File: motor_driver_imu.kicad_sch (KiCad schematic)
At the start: 27 parts, among them M1 Motor_DC, M2 Motor_DC, M3 Motor_DC, M4 Motor_DC, Q1 AO3400A, Q2 AO3400A, Q3 AO3400A, Q4 AO3400A, U5 ICM-45605

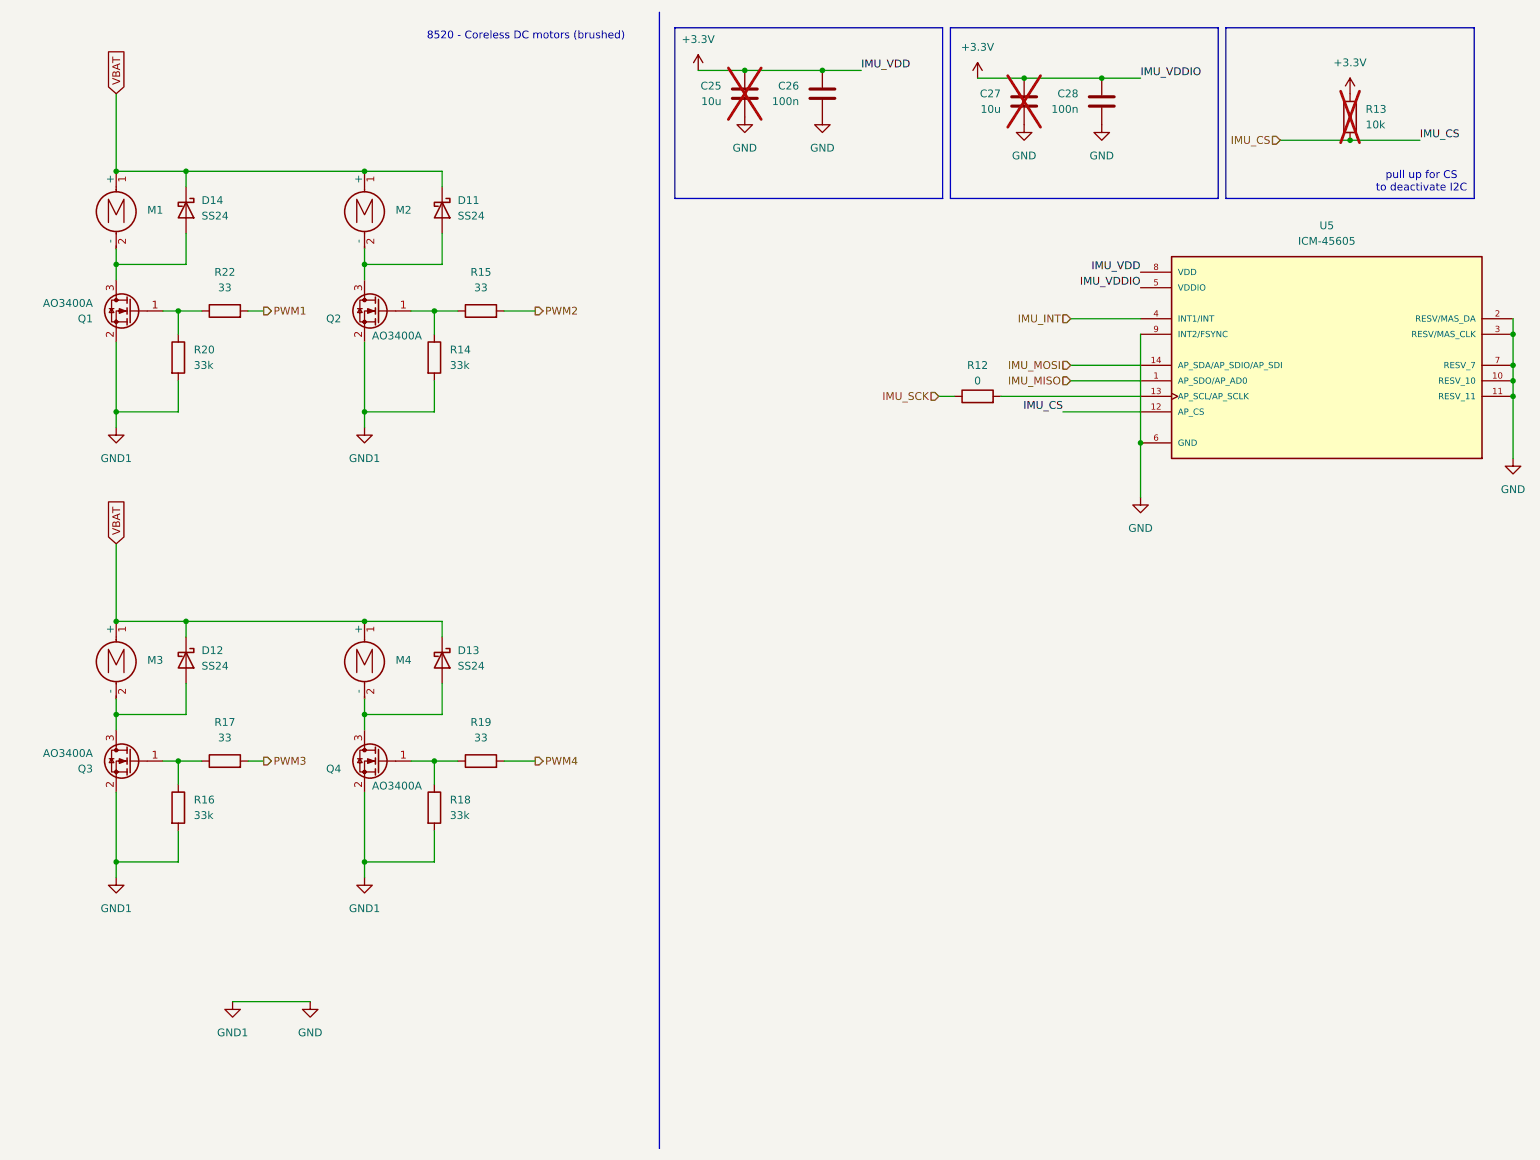
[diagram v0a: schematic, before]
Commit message: added 3.3 header for rx and changed flywheel diodes
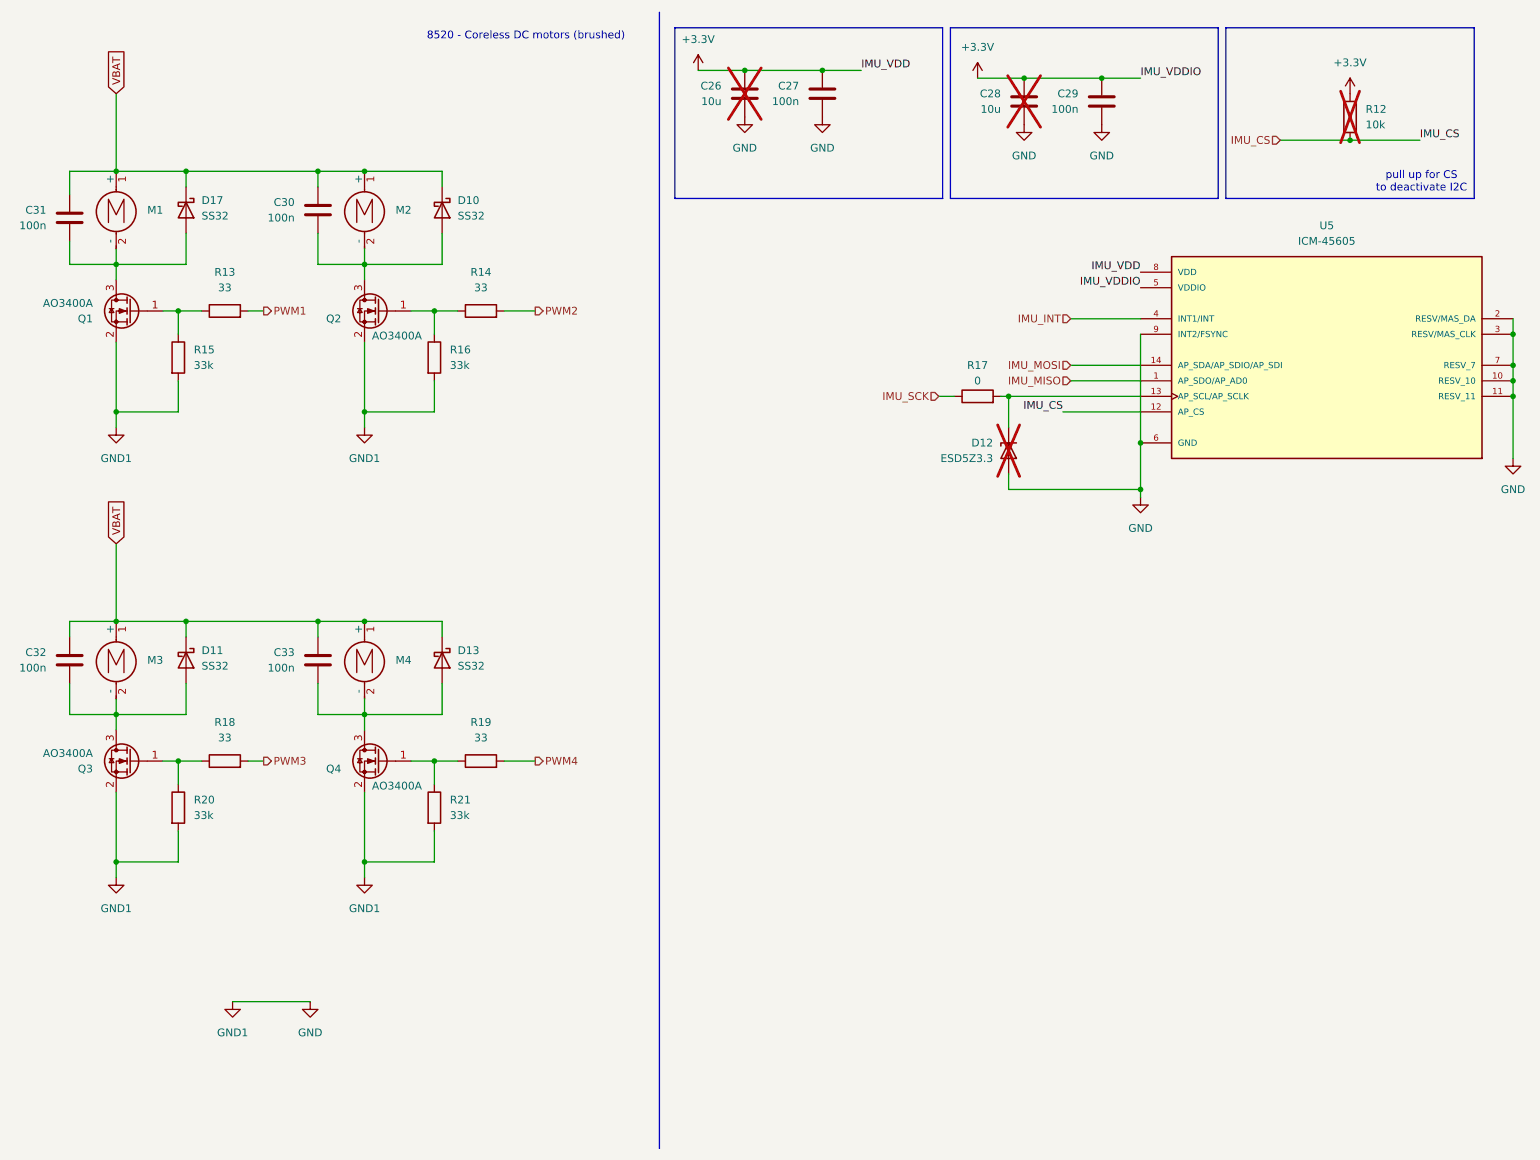
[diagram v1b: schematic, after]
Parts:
- removed D11, D12, D13, D14: SS24, Diode_SMD:D_SMA, symbol Diode:SS24
- added C30, C31, C32, C33: 100n, symbol Device:C
- added D10, D11, D13, D17: SS32, Diode_SMD:D_SMA, symbol Diode:SS32
- added D12: ESD5Z3.3, Diode_SMD:D_SOD-523, symbol Diode:ESD5Zxx
- renumbered C25 to C26, C26 to C27, C27 to C28, C28 to C29, R13 to R12, R22 to R13, R15 to R14, R20 to R15, R14 to R16, R12 to R17, R17 to R18, R16 to R20, R18 to R21
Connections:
- net GND: now also D12.2 (A)
- net VBAT: now also C30.1, C31.1, C32.1, C33.1, D10.1 (K), D11.1 (K), D13.1 (K), D17.1 (K)
- net at M2.2 (-), Q2.3 (D): now also C30.2, D10.2 (A)
- net at M3.2 (-), Q3.3 (D): now also C32.2, D11.2 (A)
- net at M1.2 (-), Q1.3 (D): now also C31.2, D17.2 (A)
- net at M4.2 (-), Q4.3 (D): now also C33.2, D13.2 (A)
- net at R17.2, U5.13 (AP_SCL/AP_SCLK): now also D12.1 (K)

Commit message: updated footprints and changed crystal
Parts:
- C26, C28, C30, C31, C32, C33: footprint (none) -> Capacitor_SMD:C_0805_2012Metric_Pad1.18x1.45mm_HandSolder
- C27, C29: footprint (none) -> Capacitor_SMD:C_0603_1608Metric_Pad1.08x0.95mm_HandSolder
- R12, R13, R14, R15, R16, R17, R18, R19, R20, R21: footprint (none) -> Resistor_SMD:R_0603_1608Metric_Pad0.98x0.95mm_HandSolder
- U5: footprint ICM-45605:XDCR_ICM-45605 -> IMU:XDCR_ICM-45605
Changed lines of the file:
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@@
 			)
 		)
-		(property "Footprint" ""
+		(property "Footprint" "Resistor_SMD:R_0603_1608Metric_Pad0.98x0.95mm_HandSolder"
 			(at 55.372 68.58 90)
 			(effects
@@
 			)
 		)
-		(property "Footprint" ""
+		(property "Footprint" "Resistor_SMD:R_0603_1608Metric_Pad0.98x0.95mm_HandSolder"
 			(at 97.282 142.24 90)
 			(effects
@@
 			)
 		)
-		(property "Footprint" ""
+		(property "Footprint" "Resistor_SMD:R_0603_1608Metric_Pad0.98x0.95mm_HandSolder"
 			(at 97.282 68.58 90)
 			(effects
@@
 			)
 		)
-		(property "Footprint" ""
+		(property "Footprint" "Capacitor_SMD:C_0603_1608Metric_Pad1.08x0.95mm_HandSolder"
 			(at 209.2452 30.48 0)
 			(effects
@@
 			)
 		)
-		(property "Footprint" ""
+		(property "Footprint" "Capacitor_SMD:C_0805_2012Metric_Pad1.18x1.45mm_HandSolder"
 			(at 40.3352 49.53 0)
 			(effects
@@
 			)
 		)
-		(property "Footprint" ""
+		(property "Footprint" "Resistor_SMD:R_0603_1608Metric_Pad0.98x0.95mm_HandSolder"
 			(at 106.68 136.398 90)
 			(effects
@@
 			)
 		)
-		(property "Footprint" ""
+		(property "Footprint" "Capacitor_SMD:C_0805_2012Metric_Pad1.18x1.45mm_HandSolder"
 			(at 80.9752 121.92 0)
 			(effects
@@
 			)
 		)
-		(property "Footprint" "ICM-45605:XDCR_ICM-45605"
+		(property "Footprint" "IMU:XDCR_ICM-45605"
 			(at 245.11 69.85 0)
 			(effects
@@
 			)
 		)
-		(property "Footprint" ""
+		(property "Footprint" "Resistor_SMD:R_0603_1608Metric_Pad0.98x0.95mm_HandSolder"
 			(at 64.77 136.398 90)
 			(effects
@@
 			)
 		)
-		(property "Footprint" ""
+		(property "Footprint" "Resistor_SMD:R_0603_1608Metric_Pad0.98x0.95mm_HandSolder"
 			(at 187.96 76.708 90)
 			(effects
@@
 			)
 		)
-		(property "Footprint" ""
+		(property "Footprint" "Capacitor_SMD:C_0805_2012Metric_Pad1.18x1.45mm_HandSolder"
 			(at 40.3352 121.92 0)
 			(effects
@@
 			)
 		)
-		(property "Footprint" ""
+		(property "Footprint" "Resistor_SMD:R_0603_1608Metric_Pad0.98x0.95mm_HandSolder"
 			(at 64.77 62.738 90)
 			(effects
@@
 			)
 		)
-		(property "Footprint" ""
+		(property "Footprint" "Capacitor_SMD:C_0805_2012Metric_Pad1.18x1.45mm_HandSolder"
 			(at 196.5452 30.48 0)
 			(effects
@@
 			)
 		)
-		(property "Footprint" ""
+		(property "Footprint" "Resistor_SMD:R_0603_1608Metric_Pad0.98x0.95mm_HandSolder"
 			(at 55.372 142.24 90)
 			(effects
@@
 			)
 		)
-		(property "Footprint" ""
+		(property "Footprint" "Capacitor_SMD:C_0805_2012Metric_Pad1.18x1.45mm_HandSolder"
 			(at 150.8252 29.21 0)
 			(effects
@@
 			)
 		)
-		(property "Footprint" ""
+		(property "Footprint" "Capacitor_SMD:C_0603_1608Metric_Pad1.08x0.95mm_HandSolder"
 			(at 163.5252 29.21 0)
 			(effects
@@
 			)
 		)
-		(property "Footprint" ""
+		(property "Footprint" "Resistor_SMD:R_0603_1608Metric_Pad0.98x0.95mm_HandSolder"
 			(at 106.68 62.738 90)
 			(effects
@@
 			)
 		)
-		(property "Footprint" ""
+		(property "Footprint" "Resistor_SMD:R_0603_1608Metric_Pad0.98x0.95mm_HandSolder"
 			(at 250.698 29.21 90)
 			(effects
@@
 			)
 		)
-		(property "Footprint" ""
+		(property "Footprint" "Capacitor_SMD:C_0805_2012Metric_Pad1.18x1.45mm_HandSolder"
 			(at 80.9752 48.26 0)
 			(effects

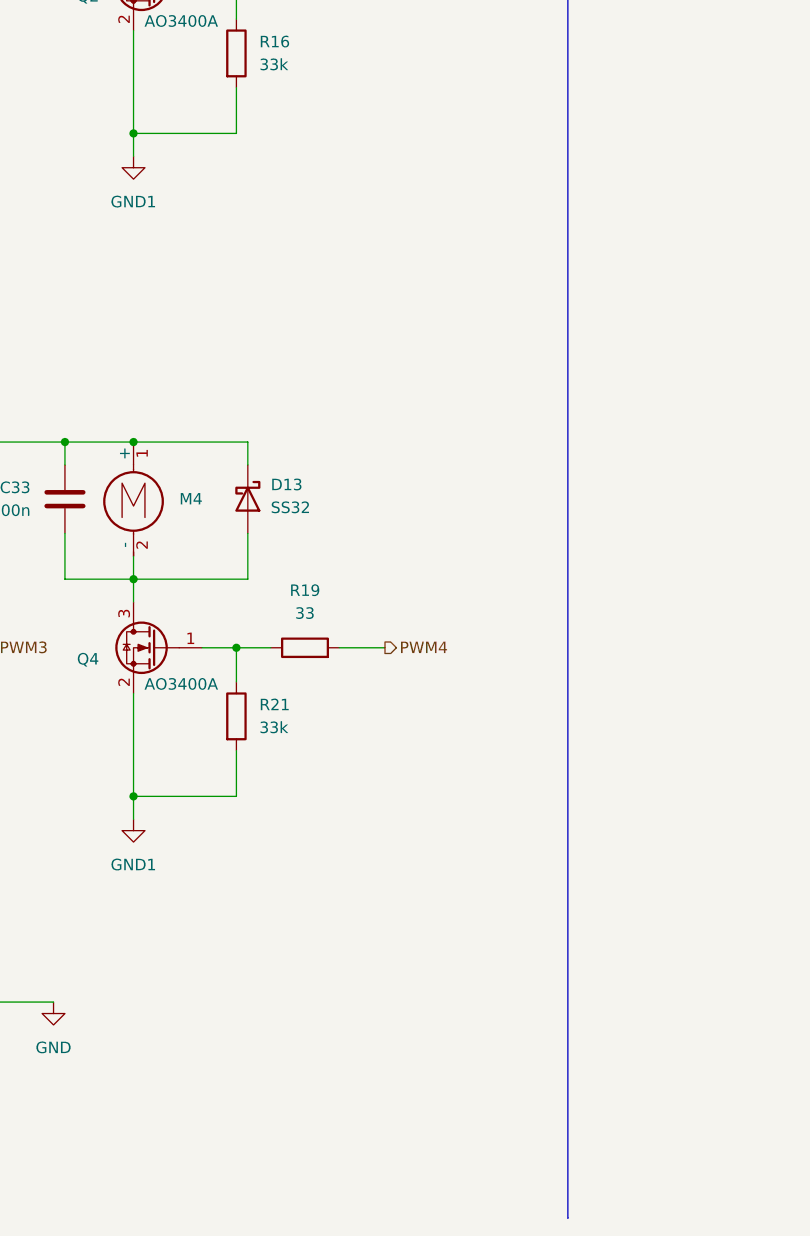
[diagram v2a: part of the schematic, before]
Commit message: added bulk cap near motors, started pcb layout routing
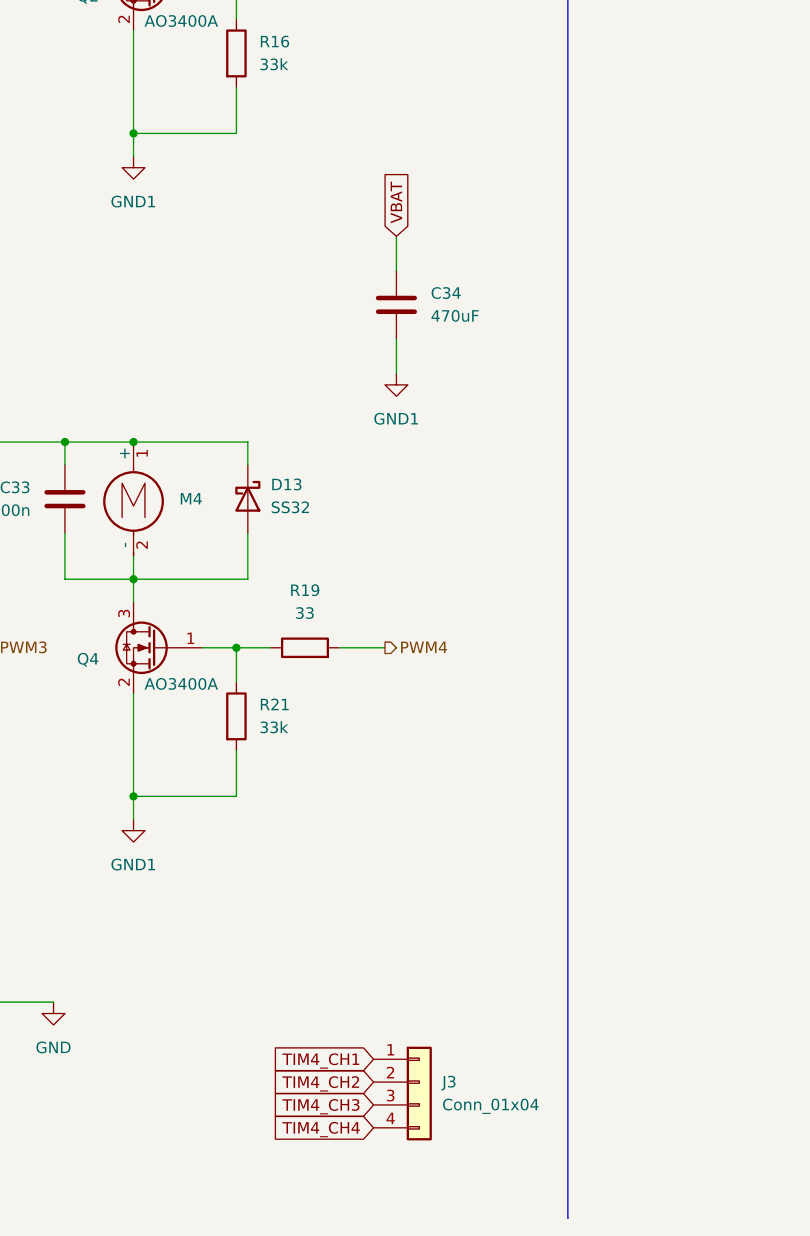
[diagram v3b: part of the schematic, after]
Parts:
- added C34: 470uF, Capacitor_THT:C_Disc_D10.0mm_W2.5mm_P5.00mm, symbol Device:C
- added J3: Conn_01x04, Connector_Wire:SolderWire-6sqmm_1x04_P14mm_D3.5mm_OD7mm, symbol Connector_Generic:Conn_01x04
- M1, M2, M3, M4: footprint (none) -> Connector_PinHeader_2.54mm:PinHeader_1x02_P2.54mm_Vertical
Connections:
- net GND: now also C34.2
- net VBAT: now also C34.1
- new net TIM4_CH1: J3.1 (Pin_1)
- new net TIM4_CH2: J3.2 (Pin_2)
- new net TIM4_CH3: J3.3 (Pin_3)
- new net TIM4_CH4: J3.4 (Pin_4)

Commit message: routed some more things
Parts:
- removed C28: 10u, Capacitor_SMD:C_0805_2012Metric_Pad1.18x1.45mm_HandSolder, symbol Device:C
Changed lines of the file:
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@@
 	)
 	(junction
-		(at 195.58 22.86)
-		(diameter 0)
-		(color 0 0 0 0)
-	)
-	(junction
 		(at 46.99 151.13)
 		(diameter 0)
@@
 	(wire
 		(pts
-			(xy 195.58 22.86) (xy 208.28 22.86)
-		)
-		(stroke
-			(width 0)
-			(type default)
-		)
-	)
-	(wire
-		(pts
-			(xy 187.96 22.86) (xy 195.58 22.86)
+			(xy 187.96 22.86) (xy 208.28 22.86)
 		)
 		(stroke
@@
 	(symbol
 		(lib_id "power:GND")
-		(at 195.58 30.48 0)
-		(unit 1)
-		(exclude_from_sim no)
-		(in_bom yes)
-		(on_board yes)
-		(dnp no)
-		(fields_autoplaced yes)
-		(property "Reference" "#PWR047"
-			(at 195.58 36.83 0)
-			(effects
-				(font
-					(size 1.27 1.27)
-				)
-				(hide yes)
-			)
-		)
-		(property "Value" "GND"
-			(at 195.58 35.56 0)
-			(effects
-				(font
-					(size 1.27 1.27)
-				)
-			)
-		)
-		(property "Footprint" ""
-			(at 195.58 30.48 0)
-			(effects
-				(font
-					(size 1.27 1.27)
-				)
-				(hide yes)
-			)
-		)
-		(property "Datasheet" ""
-			(at 195.58 30.48 0)
-			(effects
-				(font
-					(size 1.27 1.27)
-				)
-				(hide yes)
-			)
-		)
-		(property "Description" "Power symbol creates a global label with name \"GND\" , ground"
-			(at 195.58 30.48 0)
-			(effects
-				(font
-					(size 1.27 1.27)
-				)
-				(hide yes)
-			)
-		)
-		(pin "1"
-		)
-		(instances
-			(project "fiddlesticks_revised"
-				(path "/556ec640-bea9-4fdd-87e6-542e7daf24cf/8cce40b3-d144-4903-8685-8d192fa06f68"
-					(reference "#PWR047")
-					(unit 1)
-				)
-			)
-		)
-	)
-	(symbol
-		(lib_id "power:GND")
 		(at 162.56 29.21 0)
 		(unit 1)
@@
 					(unit 1)
 				)
-			)
-		)
-	)
-	(symbol
-		(lib_id "Device:C")
-		(at 195.58 26.67 0)
-		(unit 1)
-		(exclude_from_sim no)
-		(in_bom yes)
-		(on_board yes)
-		(dnp yes)
-		(property "Reference" "C28"
-			(at 191.77 25.3999 0)
-			(effects
-				(font
-					(size 1.27 1.27)
-				)
-				(justify right)
-			)
-		)
-		(property "Value" "10u"
-			(at 191.77 27.9399 0)
-			(effects
-				(font
-					(size 1.27 1.27)
-				)
-				(justify right)
-			)
-		)
-		(property "Footprint" "Capacitor_SMD:C_0805_2012Metric_Pad1.18x1.45mm_HandSolder"
-			(at 196.5452 30.48 0)
-			(effects
-				(font
-					(size 1.27 1.27)
-				)
-				(hide yes)
-			)
-		)
-		(property "Datasheet" "~"
-			(at 195.58 26.67 0)
-			(effects
-				(font
-					(size 1.27 1.27)
-				)
-				(hide yes)
-			)
-		)
-		(property "Description" "Unpolarized capacitor"
-			(at 195.58 26.67 0)
-			(effects
-				(font
-					(size 1.27 1.27)
-				)
-				(hide yes)
-			)
-		)
-		(pin "2"
-		)
-		(pin "1"
-		)
-		(instances
-			(project "fiddlesticks_revised"
-				(path "/556ec640-bea9-4fdd-87e6-542e7daf24cf/8cce40b3-d144-4903-8685-8d192fa06f68"
-					(reference "C28")
-					(unit 1)
-				)

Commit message: finished routing
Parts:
- removed J3: Conn_01x04, Connector_Wire:SolderWire-6sqmm_1x04_P14mm_D3.5mm_OD7mm, symbol Connector_Generic:Conn_01x04
- removed U5: ICM-45605, IMU:XDCR_ICM-45605, symbol IMU:ICM-45605
- added MT1: ICM-42670-P, IMU:XDCR_ICM-42670-P, symbol IMU:ICM-42670-P
- C26: value 10u -> 2.2uF; now fitted
- C29: value 100n -> 10nF
- M1, M2, M3, M4: now not fitted
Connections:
- net +3.3V: now also MT1.5 (VDDIO), MT1.8 (VDD)
- net GND: now also MT1.10 (RESV), MT1.11 (RESV), MT1.2 (RESV), MT1.3 (RESV), MT1.6 (GND), MT1.7 (FSYNC)
- net IMU_CS: now also MT1.12 (AP_CS)
- net IMU_INT: now also MT1.4 (INT1/INT)
- net IMU_MISO: now also MT1.1 (AP_SDO/AP_AD0)
- net IMU_MOSI: now also MT1.14 (AP_SDA/AP_SDIO/AP_SDI)
- net IMU_SCK: now also R17.2; no longer R17.1
- net at D12.1 (K): now also R17.1, MT1.13 (AP_SCL/AP_SCLK); no longer R17.2
- no-connect marks 0 -> 1
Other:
- moved on the sheet: D12, R17
